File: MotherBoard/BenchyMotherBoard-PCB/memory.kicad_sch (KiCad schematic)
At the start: 68 parts, among them U1 STM32MP157FAB1, U11 IS43TR16256B-125KBLI

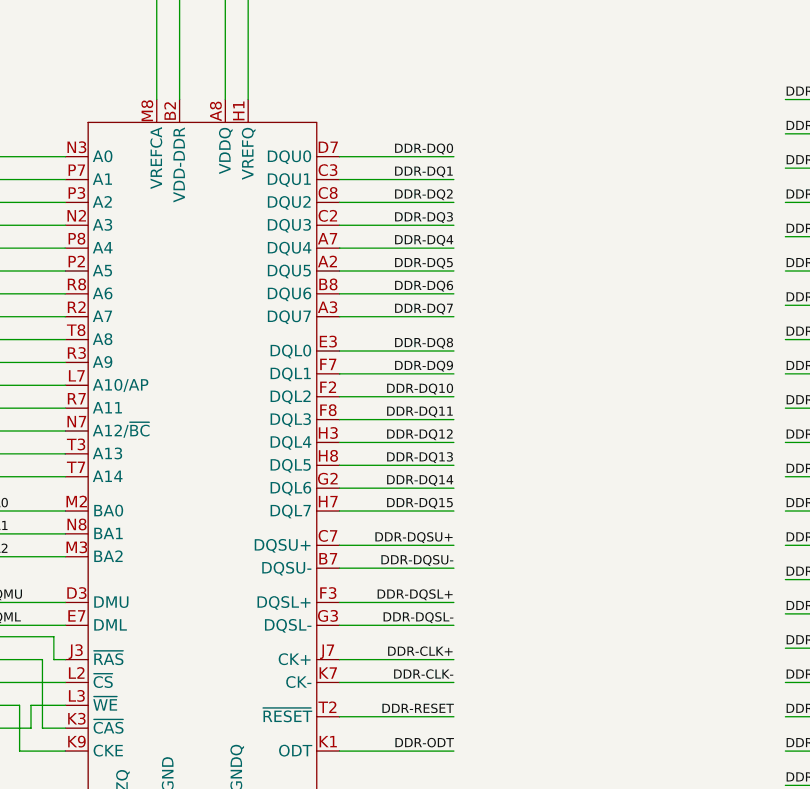
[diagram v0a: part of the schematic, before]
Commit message: Remove old DDR traces, start rerouting
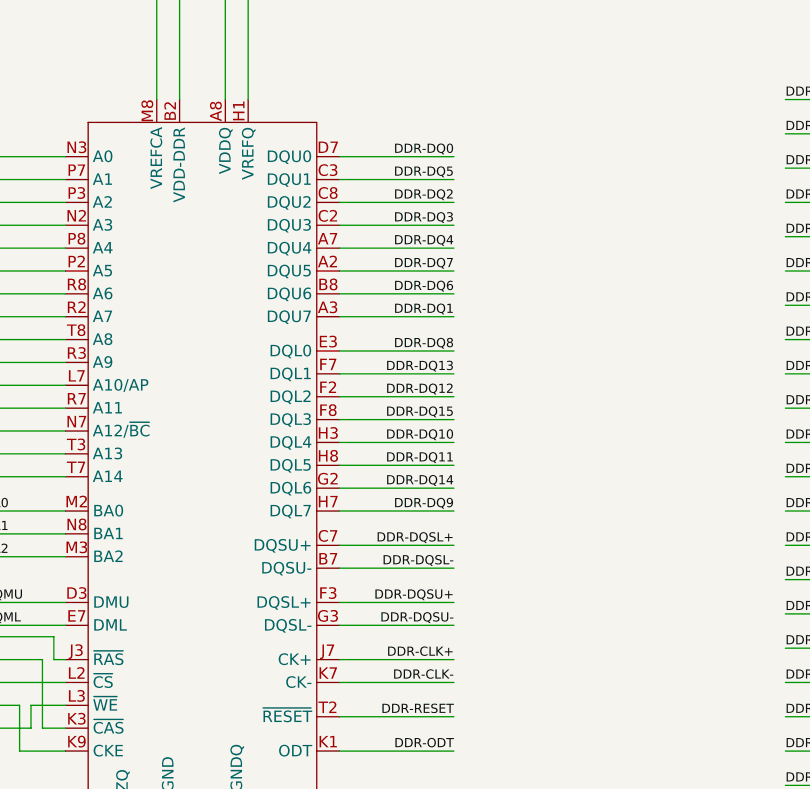
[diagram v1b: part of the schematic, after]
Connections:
- net DDR-DQ1: now also U11.A3 (DQU7); no longer U11.C3 (DQU1)
- net DDR-DQ10: now also U11.H3 (DQL4); no longer U11.F2 (DQL2)
- net DDR-DQ11: now also U11.H8 (DQL5); no longer U11.F8 (DQL3)
- net DDR-DQ12: now also U11.F2 (DQL2); no longer U11.H3 (DQL4)
- net DDR-DQ13: now also U11.F7 (DQL1); no longer U11.H8 (DQL5)
- net DDR-DQ15: now also U11.F8 (DQL3); no longer U11.H7 (DQL7)
- net DDR-DQ5: now also U11.C3 (DQU1); no longer U11.A2 (DQU5)
- net DDR-DQ7: now also U11.A2 (DQU5); no longer U11.A3 (DQU7)
- net DDR-DQ9: now also U11.H7 (DQL7); no longer U11.F7 (DQL1)
- net DDR-DQSL+: now also U11.C7 (DQSU+); no longer U11.F3 (DQSL+)
- net DDR-DQSL-: now also U11.B7 (DQSU-); no longer U11.G3 (DQSL-)
- net DDR-DQSU+: now also U11.F3 (DQSL+); no longer U11.C7 (DQSU+)
- net DDR-DQSU-: now also U11.G3 (DQSL-); no longer U11.B7 (DQSU-)
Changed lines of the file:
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@@
     (effects (font (size 1.016 1.016)) (justify left bottom))
   )
-  (label "DDR-DQ5" (at 339.09 99.06 180) (fields_autoplaced)
+  (label "DDR-DQ5" (at 339.09 88.9 180) (fields_autoplaced)
     (effects (font (size 1.016 1.016)) (justify right bottom))
   )
@@
     (effects (font (size 1.016 1.016)) (justify right bottom))
   )
-  (label "DDR-DQ11" (at 339.09 115.57 180) (fields_autoplaced)
+  (label "DDR-DQ11" (at 339.09 120.65 180) (fields_autoplaced)
     (effects (font (size 1.016 1.016)) (justify right bottom))
   )
@@
     (effects (font (size 1.016 1.016)) (justify right bottom))
   )
-  (label "DDR-DQSU-" (at 339.09 132.08 180) (fields_autoplaced)
+  (label "DDR-DQSU-" (at 339.09 138.43 180) (fields_autoplaced)
     (effects (font (size 1.016 1.016)) (justify right bottom))
   )
@@
     (effects (font (size 1.016 1.016)) (justify left bottom))
   )
-  (label "DDR-DQSL+" (at 339.09 135.89 180) (fields_autoplaced)
+  (label "DDR-DQSL+" (at 339.09 129.54 180) (fields_autoplaced)
     (effects (font (size 1.016 1.016)) (justify right bottom))
   )
@@
     (effects (font (size 1.016 1.016)) (justify left bottom))
   )
-  (label "DDR-DQ13" (at 339.09 120.65 180) (fields_autoplaced)
+  (label "DDR-DQ13" (at 339.09 110.49 180) (fields_autoplaced)
     (effects (font (size 1.016 1.016)) (justify right bottom))
   )
@@
     (effects (font (size 1.016 1.016)) (justify left bottom))
   )
-  (label "DDR-DQ12" (at 339.09 118.11 180) (fields_autoplaced)
+  (label "DDR-DQ12" (at 339.09 113.03 180) (fields_autoplaced)
     (effects (font (size 1.016 1.016)) (justify right bottom))
   )
@@
     (effects (font (size 1.016 1.016)) (justify left bottom))
   )
-  (label "DDR-DQ7" (at 339.09 104.14 180) (fields_autoplaced)
+  (label "DDR-DQ7" (at 339.09 99.06 180) (fields_autoplaced)
     (effects (font (size 1.016 1.016)) (justify right bottom))
   )
@@
     (effects (font (size 1.016 1.016)) (justify left bottom))
   )
-  (label "DDR-DQSL-" (at 339.09 138.43 180) (fields_autoplaced)
+  (label "DDR-DQSL-" (at 339.09 132.08 180) (fields_autoplaced)
     (effects (font (size 1.016 1.016)) (justify right bottom))
   )
@@
     (effects (font (size 1.016 1.016)) (justify left bottom))
   )
-  (label "DDR-DQ15" (at 339.09 125.73 180) (fields_autoplaced)
+  (label "DDR-DQ15" (at 339.09 115.57 180) (fields_autoplaced)
     (effects (font (size 1.016 1.016)) (justify right bottom))
   )
@@
     (effects (font (size 1.016 1.016)) (justify right bottom))
   )
-  (label "DDR-DQSU+" (at 339.09 129.54 180) (fields_autoplaced)
+  (label "DDR-DQSU+" (at 339.09 135.89 180) (fields_autoplaced)
     (effects (font (size 1.016 1.016)) (justify right bottom))
   )
@@
     (effects (font (size 1.016 1.016)) (justify left bottom))
   )
-  (label "DDR-DQ10" (at 339.09 113.03 180) (fields_autoplaced)
-    (effects (font (size 1.016 1.016)) (justify right bottom))
-  )
-  (label "DDR-DQ9" (at 339.09 110.49 180) (fields_autoplaced)
+  (label "DDR-DQ10" (at 339.09 118.11 180) (fields_autoplaced)
+    (effects (font (size 1.016 1.016)) (justify right bottom))
+  )
+  (label "DDR-DQ9" (at 339.09 125.73 180) (fields_autoplaced)
     (effects (font (size 1.016 1.016)) (justify right bottom))
   )
@@
     (effects (font (size 1.016 1.016)) (justify left bottom))
   )
-  (label "DDR-DQ1" (at 339.09 88.9 180) (fields_autoplaced)
-    (effects (font (size 1.016 1.016)) (justify right bottom))
-  )
+  (label "DDR-DQ1" (at 339.09 104.14 180) (fields_autoplaced)
+    (effects (font (size 1.016 1.016)) (justify right bottom))
+  )

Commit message: Initial DDR routing, start fixing skew
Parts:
- U1: footprint Daxxn_Packages:LFBGA354-P0.8mm -> Daxxn_Packages:LFBGA354-P0.8mm-STM32MP157F
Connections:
- net VDD-DDR is gone; now on net GND: C101.1, C102.1, C103.1, C104.1, C106.1, C107.1, C108.1, C109.1, C110.1, C127.1, C128.1, C129.1, C130.1, C131.1, C132.1, C133.1, C134.1, C135.1, C136.1, U11.A1 (VDDQ), U11.A8 (VDDQ), U11.B2 (VDD-DDR), U11.C1 (VDDQ), U11.C9 (VDDQ), U11.D2 (VDDQ), U11.D9 (VDD-DDR), U11.E9 (VDDQ), U11.F1 (VDDQ), U11.G7 (VDD-DDR), U11.H2 (VDDQ), U11.H9 (VDDQ), U11.K2 (VDD-DDR), U11.K8 (VDD-DDR), U11.N9 (VDD-DDR), U11.R1 (VDD-DDR), U11.R9 (VDD-DDR)
- net GND: now also U11.J1 (NC), U11.J9 (NC)
- net at U11.L1 (NC), U11.L9 (NC), U11.M7 (NC): no longer U11.J1 (NC), U11.J9 (NC)
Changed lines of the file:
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@@
       (effects (font (size 1.27 1.27)) (justify right))
     )
-    (property "Footprint" "Daxxn_Packages:LFBGA354-P0.8mm" (at 252.73 69.85 0)
+    (property "Footprint" "Daxxn_Packages:LFBGA354-P0.8mm-STM32MP157F" (at 252.73 69.85 0)
       (effects (font (size 1.27 1.27)) (justify left) hide)
     )

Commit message: Replace USB TVS W/ custom & finish DDR data layout
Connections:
- net GND: no longer C101.1, C102.1, C103.1, C104.1, C106.1, C107.1, C108.1, C109.1, C110.1, C127.1, C128.1, C129.1, C130.1, C131.1, C132.1, C133.1, C134.1, C135.1, C136.1, U11.A1 (VDDQ), U11.A8 (VDDQ), U11.B2 (VDD-DDR), U11.C1 (VDDQ), U11.C9 (VDDQ), U11.D2 (VDDQ), U11.D9 (VDD-DDR), U11.E9 (VDDQ), U11.F1 (VDDQ), U11.G7 (VDD-DDR), U11.H2 (VDDQ), U11.H9 (VDDQ), U11.J9 (NC), U11.K2 (VDD-DDR), U11.K8 (VDD-DDR), U11.N9 (VDD-DDR), U11.R1 (VDD-DDR), U11.R9 (VDD-DDR)
- new net VDD-DDR: C101.1, C102.1, C103.1, C104.1, C106.1, C107.1, C108.1, C109.1, C110.1, C127.1, C128.1, C129.1, C130.1, C131.1, C132.1, C133.1, C134.1, C135.1, C136.1, U11.A1 (VDDQ), U11.A8 (VDDQ), U11.B2 (VDD-DDR), U11.C1 (VDDQ), U11.C9 (VDDQ), U11.D2 (VDDQ), U11.D9 (VDD-DDR), U11.E9 (VDDQ), U11.F1 (VDDQ), U11.G7 (VDD-DDR), U11.H2 (VDDQ), U11.H9 (VDDQ), U11.J9 (VDD-DDR), U11.K2 (VDD-DDR), U11.K8 (VDD-DDR), U11.N9 (VDD-DDR), U11.R1 (VDD-DDR), U11.R9 (VDD-DDR)

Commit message: Add volt meter PCB
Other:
- note added: "DDR DECOUPLING"
- note added: "DDR MEMORY"
- note added: "MEMORY TERMINATION"
- moved on the sheet: C100, C101, C102, C103, C104, C105, C106, C107, C108, C109, C110, C111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
